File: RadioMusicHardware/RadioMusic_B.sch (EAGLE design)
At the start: 31 parts, among them IC4 TL074, U1 TEENSY_3.1_TW

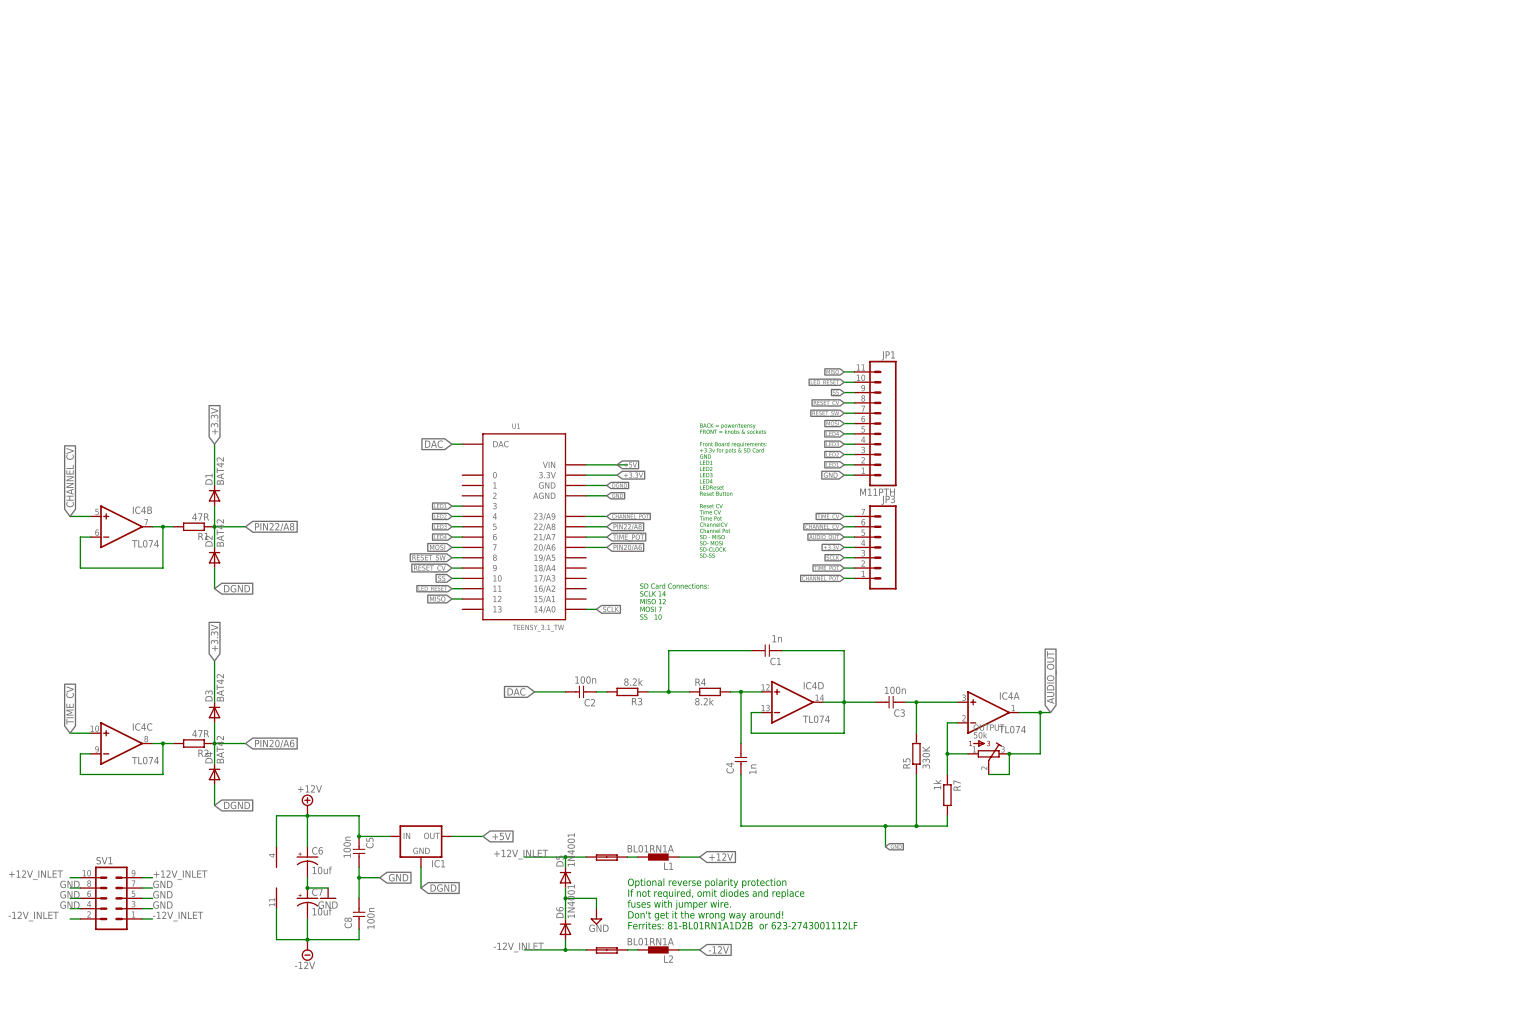
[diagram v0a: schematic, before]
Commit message: WIP on a SAMD51 back board.
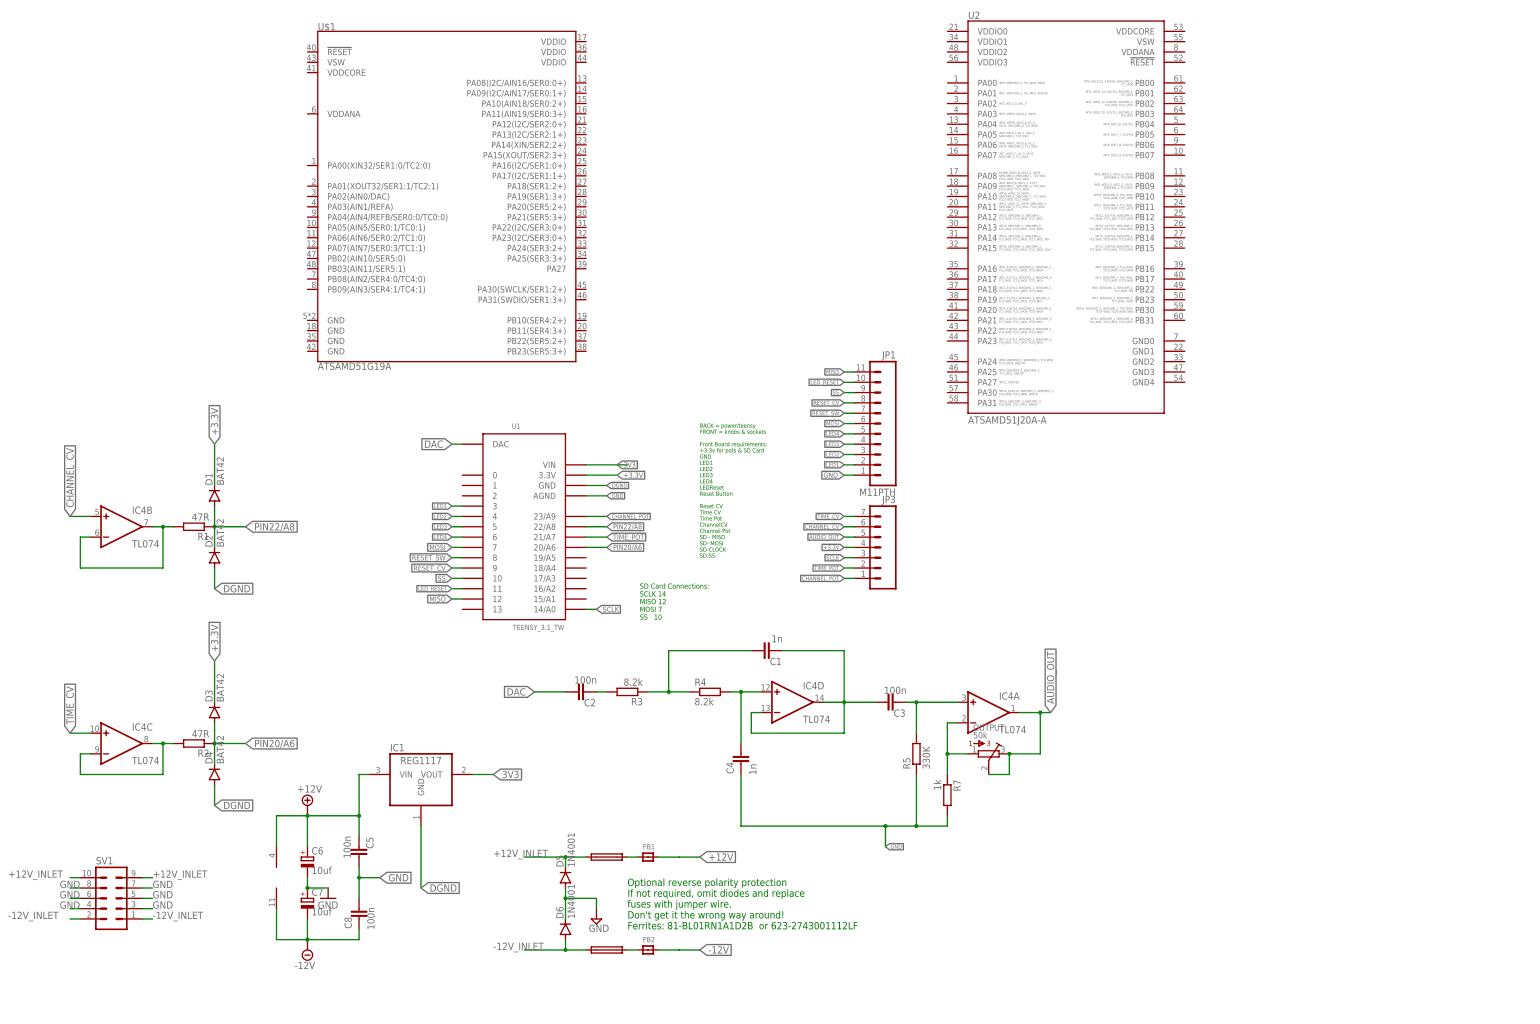
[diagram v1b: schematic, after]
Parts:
- removed L1, L2: BL01RN1A, inductors:BL01RN1A
- added FB1, FB2: (no value), microbuilder:FERRITE_0805
- added U$1: ATSAMD51G19A, SparkFun-IC-Microcontroller:ATSAMD51G19A
- added U2: ATSAMD51J20A-A, SparkFun-IC-Microcontroller:ATSAMD51J20A-A
- C1, C4, C5, C8: device TomW:C-EU050-024X044 -> rcl:C-EUC0603
- C2, C3: device TomW:C-EU050-025X075 -> rcl:C-EUC0603
- C6, C7: device SparkFun-Passives:CAP_POLPTH2 -> rcl:CPOL-EUB
- D1, D2, D3, D4: device diode:BAT81 -> diode:DIODE-SOD123
- D5, D6: device diode:1N4004 -> diode:DIODE-SOD123
- F1, F2: device TomW:PTC_FUSEPOLY_FUSE -> _JC:FUSE
- IC1: value (none) -> REG1117; device v-reg:78LXX -> burr-brown:REG1117
- IC4: device linear:TL074P -> Foxfield:TL074_SMD
- R1, R2, R3, R4, R5, R7: device TomW:R-EU_STANDARD_RESISTOR -> rcl:R-EU_R0603
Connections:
- removed net +5V: IC1.OUT, U1.VIN
- new net 3V3: IC1.VOUT, U1.VIN
- net +12V: now also FB1.P$2, IC1.VIN; no longer IC1.IN, L1.1
- net +12V_INLET: now also F1.1; no longer F1.P$1
- net -12V: now also FB2.P$2; no longer L2.1
- net -12V_INLET: now also F2.1; no longer F2.P$1
- net N$22: now also F1.2, FB1.P$1; no longer F1.P$2, L1.2
- net N$23: now also F2.2, FB2.P$1; no longer F2.P$2, L2.2

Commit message: Rear Board for SAMD51.
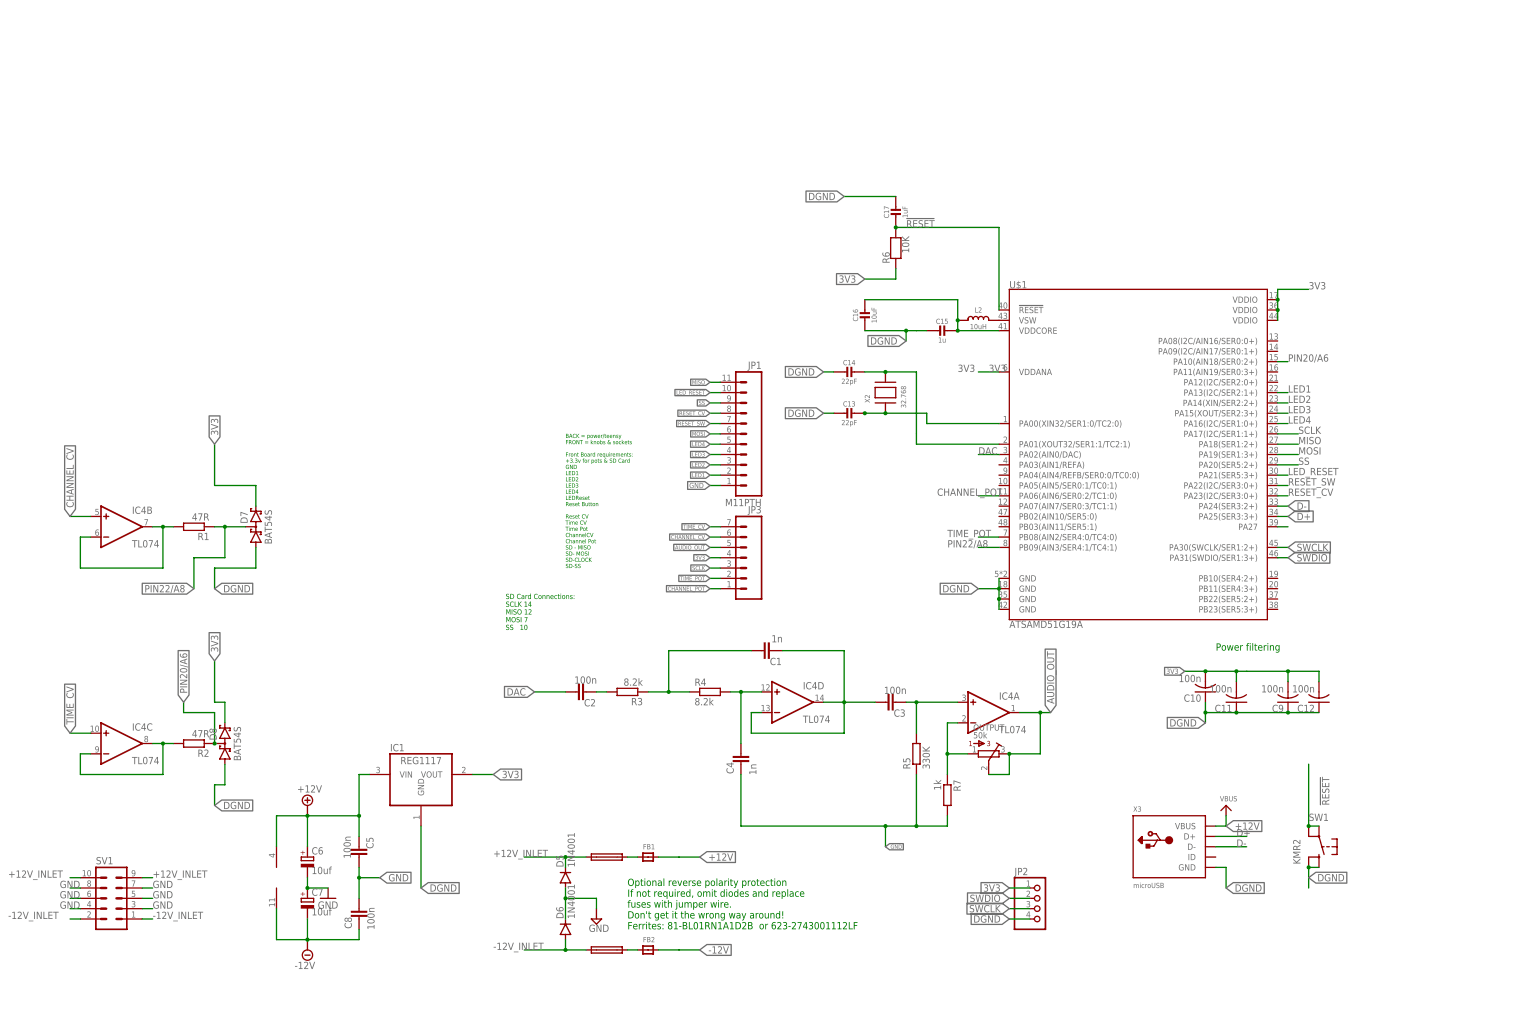
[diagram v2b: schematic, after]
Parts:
- removed D1, D2, D3, D4: BAT42, diode:DIODE-SOD123
- removed U1: TEENSY_3.1_TW, TomW:TEENSY_3.1_TW
- removed U2: ATSAMD51J20A-A, SparkFun-IC-Microcontroller:ATSAMD51J20A-A
- added C10, C11, C12, C9: 100n, adafruit:C-USC0603
- added C13, C14: 22pF, microbuilder:CAP_CERAMIC0603_NO
- added C15: 1u, microbuilder:CAP_CERAMIC0603_NO
- added C16: 10uF, microbuilder:CAP_CERAMIC0805-NOOUTLINE
- added C17: 1uF, microbuilder:CAP_CERAMIC0603_NO
- added D7, D8: BAT54S, diode:BAT54S
- added JP2: (no value), pinhead:PINHD-1X4
- added L2: 10uH, microbuilder:INDUCTOR
- added R6: 10K, microbuilder:RESISTOR_0603_NOOUT
- added SW1: KMR2, microbuilder:SWITCH_TACT_SMT4.6X2.8
- added X2: 32.768, adafruit2:XTAL-3.2X1.5
- added X3: microUSB, microbuilder:USB_MICRO_20329_V2
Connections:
- removed net +3.3V: D1.C, D3.C, JP3.4, U1.3.3V
- new net !RESET: C17.2, R6.2, SW1.P, SW1.P1, U$1.!RESET!
- new net D+: U$1.PA25(SER3:3+), X3.D+
- new net D-: U$1.PA24(SER3:2+), X3.D-
- new net N$11: L2.2, U$1.VSW
- new net N$13: U$1.PA27
- new net N$8: C13.1, U$1.PA00(XIN32/SER1:0/TC2:0), X2.P$1
- new net N$9: C14.1, U$1.PA01(XOUT32/SER1:1/TC2:1), X2.P$2
- new net SWCLK: JP2.3, U$1.PA30(SWCLK/SER1:2+)
- new net SWDIO: JP2.2, U$1.PA31(SWDIO/SER1:3+)
- net +12V: now also X3.VBUS
- net 3V3: now also C10.2, C11.2, C12.2, C15.1, C16.1, C9.2, D7.C2, D8.C2, JP2.1, JP3.4, L2.1, R6.1, U$1.VDDANA, U$1.VDDCORE, U$1.VDDIO@17, U$1.VDDIO@36, U$1.VDDIO@44; no longer U1.VIN
- net CHANNEL_POT: now also U$1.PA06(AIN6/SER0:2/TC1:0); no longer U1.23/A9
- net DAC: now also U$1.PA02(AIN0/DAC); no longer U1.DAC
- net DGND: now also C10.1, C11.1, C12.1, C13.2, C14.2, C15.2, C16.2, C17.1, C9.1, D7.A1, D8.A1, JP2.4, SW1.S, SW1.S1, U$1.GND@18, U$1.GND@35, U$1.GND@42, U$1.GND@5, X3.GND; no longer D2.A, D4.A, U1.GND
- net GND: no longer U1.AGND
- net LED1: now also U$1.PA13(I2C/SER2:1+); no longer U1.3
- net LED2: now also U$1.PA14(XIN/SER2:2+); no longer U1.4
- net LED3: now also U$1.PA15(XOUT/SER2:3+); no longer U1.5
- net LED4: now also U$1.PA16(I2C/SER1:0+); no longer U1.6
- net LED_RESET: now also U$1.PA21(SER5:3+); no longer U1.11
- net MISO: now also U$1.PA18(SER1:2+); no longer U1.12
- net MOSI: now also U$1.PA19(SER1:3+); no longer U1.7
- net PIN20/A6: now also D8.C1A2, U$1.PA10(AIN18/SER0:2+); no longer D3.A, D4.C, U1.20/A6
- net PIN22/A8: now also D7.C1A2, U$1.PB09(AIN3/SER4:1/TC4:1); no longer D1.A, D2.C, U1.22/A8
- net RESET_CV: now also U$1.PA23(I2C/SER3:0+); no longer U1.9
- net RESET_SW: now also U$1.PA22(I2C/SER3:0+); no longer U1.8
- net SCLK: now also U$1.PA17(I2C/SER1:1+); no longer U1.14/A0
- net SS: now also U$1.PA20(SER5:2+); no longer U1.10
- net TIME_POT: now also U$1.PB08(AIN2/SER4:0/TC4:0); no longer U1.21/A7
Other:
- note added: "Power filtering"
- moved on the sheet: JP1, JP3, U$1

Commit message: Connect DGND/GND via inductor. Tidy silking.
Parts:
- added L1: 10uH, microbuilder:INDUCTOR
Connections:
- net DGND: now also L1.2
- net GND: now also L1.1
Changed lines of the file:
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@@
 <part name="C17" library="microbuilder" deviceset="CAP_CERAMIC" device="0603_NO" value="1uF"/>
 <part name="JP2" library="pinhead" library_urn="urn:adsk.eagle:library:325" deviceset="PINHD-1X4" device="" package3d_urn="urn:adsk.eagle:package:22407/2"/>
+<part name="L1" library="microbuilder" deviceset="INDUCTOR" device="" value="10uH"/>
 </parts>
 <sheets>
@@
 <attribute name="VALUE" x="237.49" y="12.7" size="1.778" layer="96"/>
 </instance>
+<instance part="L1" gate="G$1" x="342.9" y="91.44" smashed="yes">
+<attribute name="NAME" x="342.9" y="93.98" size="1.27" layer="95" align="center"/>
+<attribute name="VALUE" x="342.9" y="89.9" size="1.27" layer="96" align="center"/>
+</instance>
 </instances>
 <busses>
@@
 <wire x1="162.56" y1="124.46" x2="165.1" y2="124.46" width="0.1524" layer="91"/>
 <label x="162.56" y="124.46" size="1.27" layer="95" rot="R180" xref="yes"/>
+</segment>
+<segment>
+<wire x1="322.58" y1="91.44" x2="337.82" y2="91.44" width="0.1524" layer="91"/>
+<pinref part="L1" gate="G$1" pin="1"/>
+<label x="322.58" y="91.44" size="1.778" layer="95" rot="R180" xref="yes"/>
 </segment>
 </net>
@@
 <label x="236.22" y="17.78" size="1.778" layer="95" rot="R180" xref="yes"/>
 </segment>
-</net>
+<segment>
+<pinref part="L1" gate="G$1" pin="2"/>
+<wire x1="347.98" y1="91.44" x2="353.06" y2="91.44" width="0.1524" layer="91"/>
+<label x="353.06" y="91.44" size="1.778" layer="95" xref="yes"/>
+</segment>
+</net>

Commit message: Rev A of MTM Brain board.
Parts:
- removed X3: microUSB, microbuilder:USB_MICRO_20329_V2
- added J1: UJ2-MIBH2-4-SMT-TR, UJ2-MIBH2-4-SMT-TR:UJ2-MIBH2-4-SMT-TR
- C10, C11, C12, C9: device adafruit:C-USC0603 -> rcl:C-EUC0603
- C16: value 10uF -> 10u
- C17: value 1uF -> 1u
- D5, D6: value 1N4001 -> S1M; device diode:DIODE-SOD123 -> diode:S1M
- renumbered U$1 to U1
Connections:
- net +12V: now also J1.VCC; no longer X3.VBUS
- net D+: now also J1.D+; no longer X3.D+
- net D-: now also J1.D-; no longer X3.D-
- net DGND: now also J1.GND, J1.SHIELD; no longer X3.GND
